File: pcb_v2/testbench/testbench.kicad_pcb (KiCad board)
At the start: 2 copper layers, 274.3 x 124.5 mm, 70 parts, among them J1 test_A, J10 test_C1, J11 test_C2, J12 test_C3, J15 lcd, J17 DEBUG, J18 power_jack, J2 test_B, J3 sub_0, J4 sub_8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

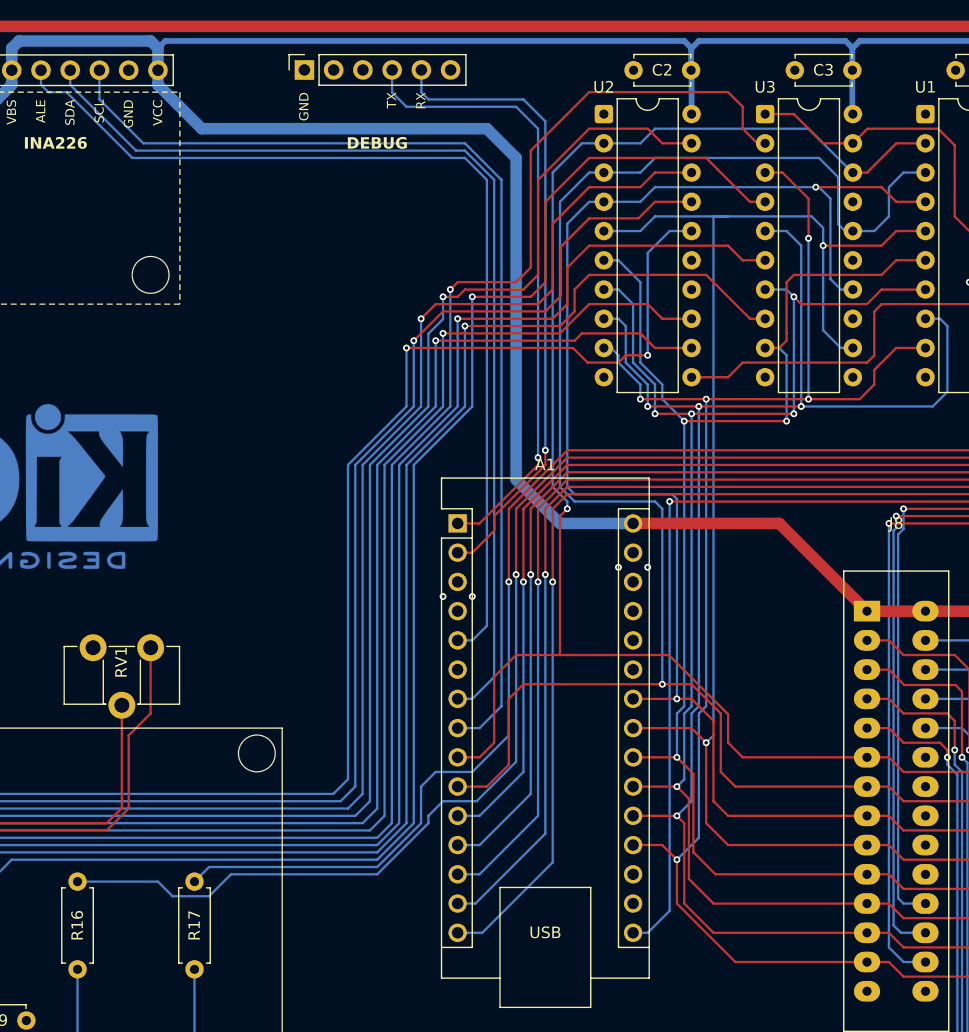
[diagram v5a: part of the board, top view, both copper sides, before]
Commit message: correcao na pinagem do INA226 (SDA e SCL entravam nos pinos errados do arduino)
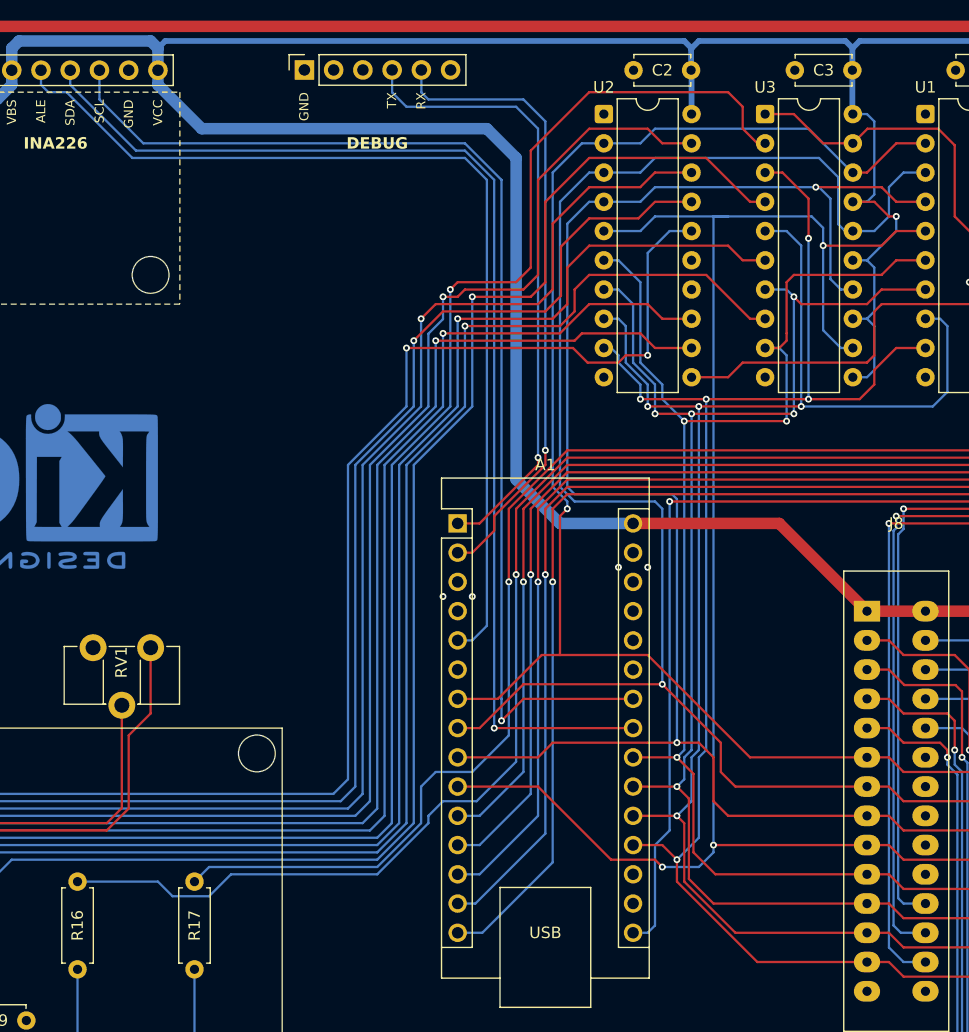
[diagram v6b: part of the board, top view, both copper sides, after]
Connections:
- A1 pad 10: mpu_data_1 -> mpu_data_3
- A1 pad 23: mpu_data_3 -> mcu_power_sda
- A1 pad 24: mpu_data_2 -> mcu_power_scl
- A1 pad 7: mcu_power_sda -> mpu_data_0
- A1 pad 8: mcu_power_scl -> mpu_data_1
- A1 pad 9: mpu_data_0 -> mpu_data_2
- U3 pad 11: unconnected-(U3-I0b-Pad11) -> +5V
- U3 pad 13: unconnected-(U3-I1b-Pad13) -> +5V
- U3 pad 15: unconnected-(U3-I2b-Pad15) -> +5V
- U3 pad 17: unconnected-(U3-I3b-Pad17) -> +5V
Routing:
- net +5V: track 612.0 -> 646.7 mm, vias 0 -> 1
- net mpu_data_3: track 186.7 -> 206.4 mm, vias 2 -> 3
- net mpu_data_2: track 191.7 -> 207.9 mm
- net mcu_power_sda: track 88.7 -> 101.2 mm, vias 0 -> 1
- net mcu_power_scl: track 90.7 -> 99.6 mm, vias 0 -> 1
- net mpu_data_1: track 209.6 -> 202.7 mm
- net mpu_data_0: track 195.1 -> 188.2 mm
- net mpu_data_7: track 192.0 -> 190.8 mm
- net mpu_data_6: track 195.5 -> 194.4 mm
